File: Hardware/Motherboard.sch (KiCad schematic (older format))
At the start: 19 parts, among them J1 Pin_Header_02x08, J2 Pin_Header_02x08, J3 Pin_Header_02x08, U1 PIC18F26K22-I-SO, U2 FT240XS, U3 TXB0104D, U4 TXB0104D

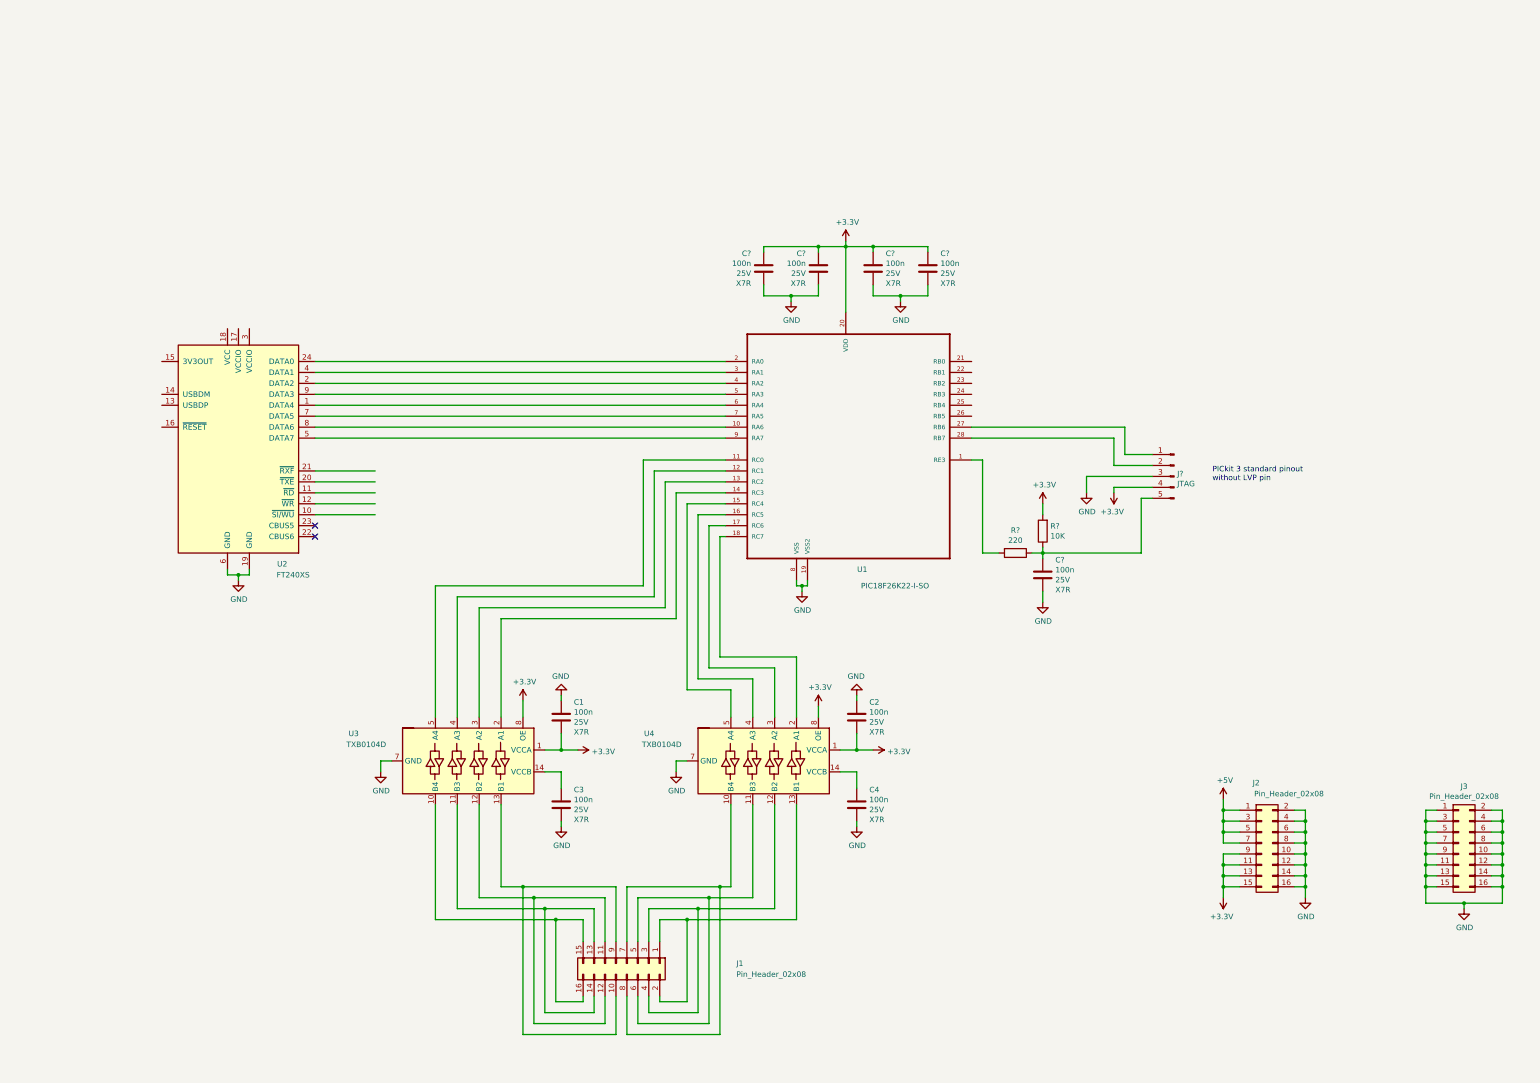
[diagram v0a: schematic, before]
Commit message: [Hardware] Added LDO and led to schematic.
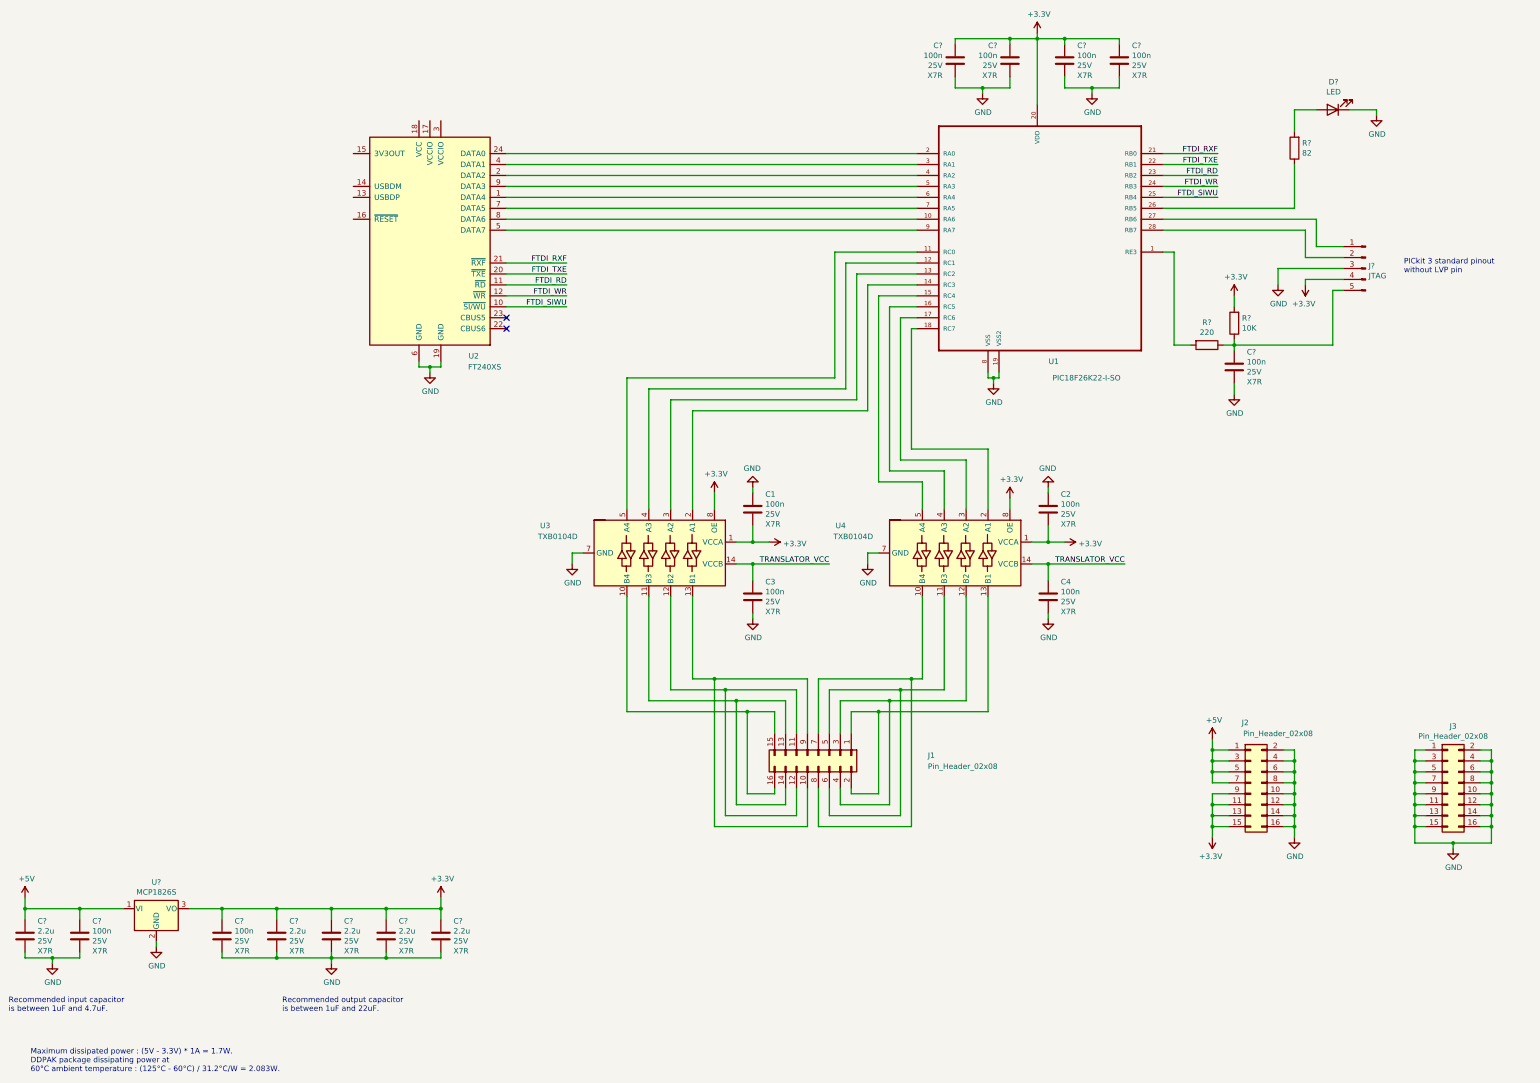
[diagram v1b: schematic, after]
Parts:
- added C? (x2): 100n, Capacitor_SMD:C_1206_3216Metric_Pad1.42x1.75mm_HandSolder, symbol Device:C
- added C? (x5): 2.2u, Capacitor_SMD:C_1206_3216Metric_Pad1.42x1.75mm_HandSolder, symbol Device:C
- added D?: LED, LED_THT:LED_D5.0mm, symbol Device:LED
- added R?: 82, Resistor_SMD:R_1206_3216Metric_Pad1.42x1.75mm_HandSolder, symbol Device:R
- added U?: MCP1826S, Package_TO_SOT_SMD:TO-263-3_TabPin2, symbol Regulator_Linear:MCP1826S
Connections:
- net +3V3: now also C?.1, C?.1, C?.1, C?.1, C?.1, U?.3 (VO)
- net +5V: now also C?.1, C?.1, U?.1 (VI)
- net GND: now also C?.2, C?.2, C?.2, C?.2, C?.2, C?.2, C?.2, D?.1 (K), U?.2 (GND)
- net FTDI_SIWU: now reaches U2.10 (~SI/WU)
- net FTDI_SIWU: now also U1.25 (RB4)
- net FTDI_RD: now reaches U2.11 (~RD)
- net FTDI_RD: now also U1.23 (RB2)
- net FTDI_WR: now reaches U2.12 (~WR)
- net FTDI_WR: now also U1.24 (RB3)
- net FTDI_TXE: now reaches U2.20 (~TXE)
- net FTDI_TXE: now also U1.22 (RB1)
- net FTDI_RXF: now reaches U2.21 (~RXF)
- net FTDI_RXF: now also U1.21 (RB0)
- net at U1.26 (RB5): now also R?.1
- net TRANSLATOR_VCC: now reaches C3.1, U3.14 (VCCB)
- net TRANSLATOR_VCC: now also C4.1, U4.14 (VCCB)
- new net: D?.2 (A), R?.2
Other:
- note added: "Maximum dissipated power : (5V - 3.3V) * 1A = 1.7W.\nDDPAK package dissipating power at\n60°C ambient temperature : (125°C - 60°C) / 31.2°C/W = 2.083W."
- note added: "Recommended input capacitor\nis between 1uF and 4.7uF."
- note added: "Recommended output capacitor\nis between 1uF and 22uF."
- moved on the sheet: C1, C2, C3, C4, C?, J1, J2, J3, J?, R?, U1, U2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

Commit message: [Hardware] Added FTDI FIFO and logic signals output voltage switch to schematic.
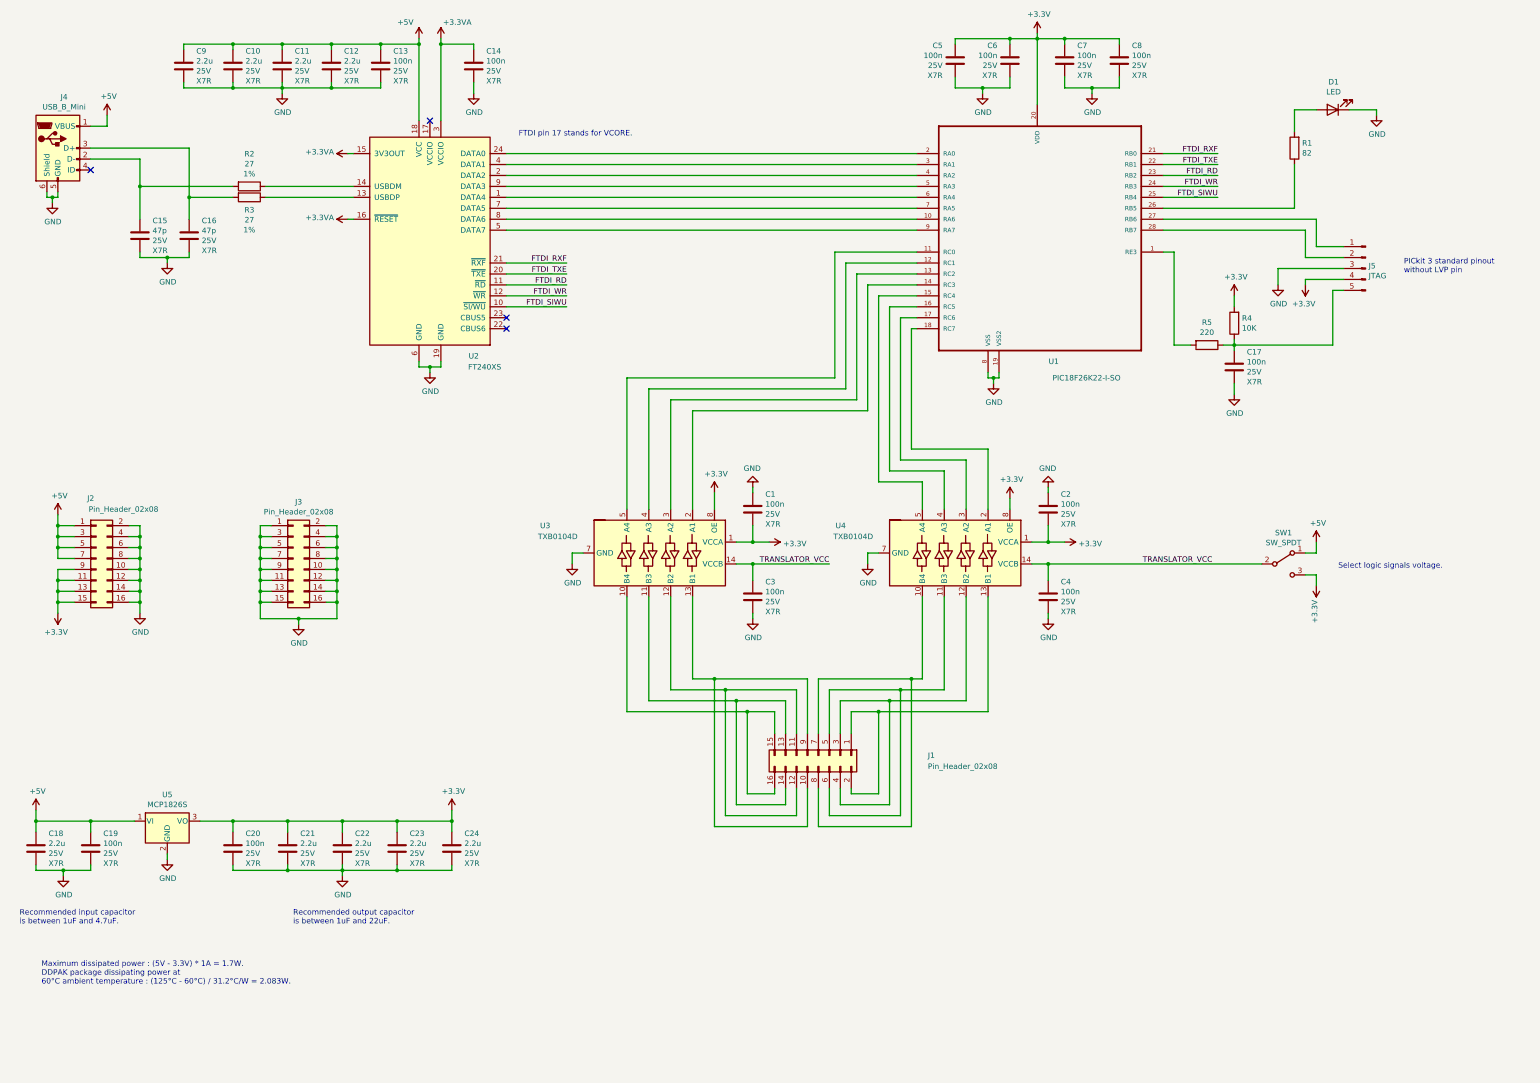
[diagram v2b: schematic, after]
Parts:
- added C10, C11, C12, C9: 2.2u, Capacitor_SMD:C_1206_3216Metric_Pad1.42x1.75mm_HandSolder, symbol Device:C
- added C13, C14: 100n, Capacitor_SMD:C_1206_3216Metric_Pad1.42x1.75mm_HandSolder, symbol Device:C
- added C15, C16: 47p, Capacitor_SMD:C_1206_3216Metric_Pad1.42x1.75mm_HandSolder, symbol Device:C
- added J4: USB_B_Mini, Connector_USB:USB_Mini-B_Lumberg_2486_01_Horizontal, symbol Connector:USB_B_Mini
- added R2, R3: 27, Resistor_SMD:R_1206_3216Metric_Pad1.42x1.75mm_HandSolder, symbol Device:R
- added SW1: SW_SPDT, Button_Switch_THT:SW_CuK_OS102011MA1QN1_SPDT_Angled, symbol Switch:SW_SPDT
- gave numbers to parts that had none: 18
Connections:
- net +3V3: now also SW1.3 (C)
- net +5V: now also U2.18 (VCC), C10.1, C11.1, C12.1, C13.1, C9.1, J4.1 (VBUS), SW1.1 (A)
- net GND: now also C10.2, C11.2, C12.2, C13.2, C14.2, C15.2, C16.2, C9.2, J4.5 (GND), J4.6 (Shield)
- net TRANSLATOR_VCC: now also SW1.2 (B)
- net at U2.13 (USBDP): now also R3.1
- net at U2.14 (USBDM): now also R2.1
- net +3.3VA: now reaches U2.15 (3V3OUT)
- net +3.3VA: now also U2.16 (~RESET), U2.3 (VCCIO), C14.1
- new net: C15.1, J4.2 (D-), R2.2
- new net: C16.1, J4.3 (D+), R3.2
- no-connect marks 2 -> 4
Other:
- note added: "FTDI pin 17 stands for VCORE."
- note added: "Select logic signals voltage."
- moved on the sheet: C18, C19, C20, C21, C22, C23, C24, J2, J3, U5

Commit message: [Hardware] Placed components on PCB.
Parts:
- C1, C10, C11, C12, C13, C14, C15, C16, C17, C18, C19, C2, C20, C21, C22, C23, C24, C3, C4, C5, C6, C7, C8, C9: footprint Capacitor_SMD:C_1206_3216Metric_Pad1.42x1.75mm_HandSolder -> Capacitor_SMD:C_0805_2012Metric_Pad1.15x1.40mm_HandSolder
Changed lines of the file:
@@
 F 0 "C2" H 11265 5887 50  0000 L CNN
 F 1 "100n" H 11265 5796 50  0000 L CNN
-F 2 "Capacitor_SMD:C_1206_3216Metric_Pad1.42x1.75mm_HandSolder" H 11188 5600 50  0001 C CNN
+F 2 "Capacitor_SMD:C_0805_2012Metric_Pad1.15x1.40mm_HandSolder" H 11188 5600 50  0001 C CNN
 F 3 "~" H 11150 5750 50  0001 C CNN
 F 4 "25V" H 11265 5705 50  0000 L CNN "Value2"
@@
 F 0 "C4" H 11265 6687 50  0000 L CNN
 F 1 "100n" H 11265 6596 50  0000 L CNN
-F 2 "Capacitor_SMD:C_1206_3216Metric_Pad1.42x1.75mm_HandSolder" H 11188 6400 50  0001 C CNN
+F 2 "Capacitor_SMD:C_0805_2012Metric_Pad1.15x1.40mm_HandSolder" H 11188 6400 50  0001 C CNN
 F 3 "~" H 11150 6550 50  0001 C CNN
 F 4 "25V" H 11265 6505 50  0000 L CNN "Value2"
@@
 F 0 "C1" H 8565 5887 50  0000 L CNN
 F 1 "100n" H 8565 5796 50  0000 L CNN
-F 2 "Capacitor_SMD:C_1206_3216Metric_Pad1.42x1.75mm_HandSolder" H 8488 5600 50  0001 C CNN
+F 2 "Capacitor_SMD:C_0805_2012Metric_Pad1.15x1.40mm_HandSolder" H 8488 5600 50  0001 C CNN
 F 3 "~" H 8450 5750 50  0001 C CNN
 F 4 "25V" H 8565 5705 50  0000 L CNN "Value2"
@@
 F 0 "C3" H 8565 6687 50  0000 L CNN
 F 1 "100n" H 8565 6596 50  0000 L CNN
-F 2 "Capacitor_SMD:C_1206_3216Metric_Pad1.42x1.75mm_HandSolder" H 8488 6400 50  0001 C CNN
+F 2 "Capacitor_SMD:C_0805_2012Metric_Pad1.15x1.40mm_HandSolder" H 8488 6400 50  0001 C CNN
 F 3 "~" H 8450 6550 50  0001 C CNN
 F 4 "25V" H 8565 6505 50  0000 L CNN "Value2"
@@
 F 0 "C7" H 11415 1787 50  0000 L CNN
 F 1 "100n" H 11415 1696 50  0000 L CNN
-F 2 "Capacitor_SMD:C_1206_3216Metric_Pad1.42x1.75mm_HandSolder" H 11338 1500 50  0001 C CNN
+F 2 "Capacitor_SMD:C_0805_2012Metric_Pad1.15x1.40mm_HandSolder" H 11338 1500 50  0001 C CNN
 F 3 "~" H 11300 1650 50  0001 C CNN
 F 4 "25V" H 11415 1605 50  0000 L CNN "Value2"
@@
 F 0 "C8" H 11915 1787 50  0000 L CNN
 F 1 "100n" H 11915 1696 50  0000 L CNN
-F 2 "Capacitor_SMD:C_1206_3216Metric_Pad1.42x1.75mm_HandSolder" H 11838 1500 50  0001 C CNN
+F 2 "Capacitor_SMD:C_0805_2012Metric_Pad1.15x1.40mm_HandSolder" H 11838 1500 50  0001 C CNN
 F 3 "~" H 11800 1650 50  0001 C CNN
 F 4 "25V" H 11915 1605 50  0000 L CNN "Value2"
@@
 F 0 "C5" H 10185 1787 50  0000 R CNN
 F 1 "100n" H 10185 1696 50  0000 R CNN
-F 2 "Capacitor_SMD:C_1206_3216Metric_Pad1.42x1.75mm_HandSolder" H 10338 1500 50  0001 C CNN
+F 2 "Capacitor_SMD:C_0805_2012Metric_Pad1.15x1.40mm_HandSolder" H 10338 1500 50  0001 C CNN
 F 3 "~" H 10300 1650 50  0001 C CNN
 F 4 "25V" H 10185 1605 50  0000 R CNN "Value2"
@@
 F 0 "C6" H 10685 1787 50  0000 R CNN
 F 1 "100n" H 10685 1696 50  0000 R CNN
-F 2 "Capacitor_SMD:C_1206_3216Metric_Pad1.42x1.75mm_HandSolder" H 10838 1500 50  0001 C CNN
+F 2 "Capacitor_SMD:C_0805_2012Metric_Pad1.15x1.40mm_HandSolder" H 10838 1500 50  0001 C CNN
 F 3 "~" H 10800 1650 50  0001 C CNN
 F 4 "25V" H 10685 1605 50  0000 R CNN "Value2"
@@
 F 0 "C17" H 12965 4587 50  0000 L CNN
 F 1 "100n" H 12965 4496 50  0000 L CNN
-F 2 "Capacitor_SMD:C_1206_3216Metric_Pad1.42x1.75mm_HandSolder" H 12888 4300 50  0001 C CNN
+F 2 "Capacitor_SMD:C_0805_2012Metric_Pad1.15x1.40mm_HandSolder" H 12888 4300 50  0001 C CNN
 F 3 "~" H 12850 4450 50  0001 C CNN
 F 4 "25V" H 12965 4405 50  0000 L CNN "Champ4"
@@
 F 0 "C19" H 2515 8987 50  0000 L CNN
 F 1 "100n" H 2515 8896 50  0000 L CNN
-F 2 "Capacitor_SMD:C_1206_3216Metric_Pad1.42x1.75mm_HandSolder" H 2438 8700 50  0001 C CNN
+F 2 "Capacitor_SMD:C_0805_2012Metric_Pad1.15x1.40mm_HandSolder" H 2438 8700 50  0001 C CNN
 F 3 "~" H 2400 8850 50  0001 C CNN
 F 4 "25V" H 2515 8805 50  0000 L CNN "Value2"
@@
 F 0 "C20" H 3815 8987 50  0000 L CNN
 F 1 "100n" H 3815 8896 50  0000 L CNN
-F 2 "Capacitor_SMD:C_1206_3216Metric_Pad1.42x1.75mm_HandSolder" H 3738 8700 50  0001 C CNN
+F 2 "Capacitor_SMD:C_0805_2012Metric_Pad1.15x1.40mm_HandSolder" H 3738 8700 50  0001 C CNN
 F 3 "~" H 3700 8850 50  0001 C CNN
 F 4 "25V" H 3815 8805 50  0000 L CNN "Value2"
@@
 F 0 "C21" H 4315 8987 50  0000 L CNN
 F 1 "2.2u" H 4315 8896 50  0000 L CNN
-F 2 "Capacitor_SMD:C_1206_3216Metric_Pad1.42x1.75mm_HandSolder" H 4238 8700 50  0001 C CNN
+F 2 "Capacitor_SMD:C_0805_2012Metric_Pad1.15x1.40mm_HandSolder" H 4238 8700 50  0001 C CNN
 F 3 "~" H 4200 8850 50  0001 C CNN
 F 4 "25V" H 4315 8805 50  0000 L CNN "Value2"
@@
 F 0 "C18" H 2015 8987 50  0000 L CNN
 F 1 "2.2u" H 2015 8896 50  0000 L CNN
-F 2 "Capacitor_SMD:C_1206_3216Metric_Pad1.42x1.75mm_HandSolder" H 1938 8700 50  0001 C CNN
+F 2 "Capacitor_SMD:C_0805_2012Metric_Pad1.15x1.40mm_HandSolder" H 1938 8700 50  0001 C CNN
 F 3 "~" H 1900 8850 50  0001 C CNN
 F 4 "25V" H 2015 8805 50  0000 L CNN "Value2"
@@
 F 0 "C22" H 4815 8987 50  0000 L CNN
 F 1 "2.2u" H 4815 8896 50  0000 L CNN
-F 2 "Capacitor_SMD:C_1206_3216Metric_Pad1.42x1.75mm_HandSolder" H 4738 8700 50  0001 C CNN
+F 2 "Capacitor_SMD:C_0805_2012Metric_Pad1.15x1.40mm_HandSolder" H 4738 8700 50  0001 C CNN
 F 3 "~" H 4700 8850 50  0001 C CNN
 F 4 "25V" H 4815 8805 50  0000 L CNN "Value2"
@@
 F 0 "C23" H 5315 8987 50  0000 L CNN
 F 1 "2.2u" H 5315 8896 50  0000 L CNN
-F 2 "Capacitor_SMD:C_1206_3216Metric_Pad1.42x1.75mm_HandSolder" H 5238 8700 50  0001 C CNN
+F 2 "Capacitor_SMD:C_0805_2012Metric_Pad1.15x1.40mm_HandSolder" H 5238 8700 50  0001 C CNN
 F 3 "~" H 5200 8850 50  0001 C CNN
 F 4 "25V" H 5315 8805 50  0000 L CNN "Value2"
@@
 F 0 "C24" H 5815 8987 50  0000 L CNN
 F 1 "2.2u" H 5815 8896 50  0000 L CNN
-F 2 "Capacitor_SMD:C_1206_3216Metric_Pad1.42x1.75mm_HandSolder" H 5738 8700 50  0001 C CNN
+F 2 "Capacitor_SMD:C_0805_2012Metric_Pad1.15x1.40mm_HandSolder" H 5738 8700 50  0001 C CNN
 F 3 "~" H 5700 8850 50  0001 C CNN
 F 4 "25V" H 5815 8805 50  0000 L CNN "Value2"
@@
 F 0 "C14" H 6015 1837 50  0000 L CNN
 F 1 "100n" H 6015 1746 50  0000 L CNN
-F 2 "Capacitor_SMD:C_1206_3216Metric_Pad1.42x1.75mm_HandSolder" H 5938 1550 50  0001 C CNN
+F 2 "Capacitor_SMD:C_0805_2012Metric_Pad1.15x1.40mm_HandSolder" H 5938 1550 50  0001 C CNN
 F 3 "~" H 5900 1700 50  0001 C CNN
 F 4 "25V" H 6015 1655 50  0000 L CNN "Value2"
@@
 F 0 "C13" H 5165 1837 50  0000 L CNN
 F 1 "100n" H 5165 1746 50  0000 L CNN
-F 2 "Capacitor_SMD:C_1206_3216Metric_Pad1.42x1.75mm_HandSolder" H 5088 1550 50  0001 C CNN
+F 2 "Capacitor_SMD:C_0805_2012Metric_Pad1.15x1.40mm_HandSolder" H 5088 1550 50  0001 C CNN
 F 3 "~" H 5050 1700 50  0001 C CNN
 F 4 "25V" H 5165 1655 50  0000 L CNN "Value2"
@@
 F 0 "C12" H 4715 1837 50  0000 L CNN
 F 1 "2.2u" H 4715 1746 50  0000 L CNN
-F 2 "Capacitor_SMD:C_1206_3216Metric_Pad1.42x1.75mm_HandSolder" H 4638 1550 50  0001 C CNN
+F 2 "Capacitor_SMD:C_0805_2012Metric_Pad1.15x1.40mm_HandSolder" H 4638 1550 50  0001 C CNN
 F 3 "~" H 4600 1700 50  0001 C CNN
 F 4 "25V" H 4715 1655 50  0000 L CNN "Value2"
@@
 F 0 "C11" H 4265 1837 50  0000 L CNN
 F 1 "2.2u" H 4265 1746 50  0000 L CNN
-F 2 "Capacitor_SMD:C_1206_3216Metric_Pad1.42x1.75mm_HandSolder" H 4188 1550 50  0001 C CNN
+F 2 "Capacitor_SMD:C_0805_2012Metric_Pad1.15x1.40mm_HandSolder" H 4188 1550 50  0001 C CNN
 F 3 "~" H 4150 1700 50  0001 C CNN
 F 4 "25V" H 4265 1655 50  0000 L CNN "Value2"
@@
 F 0 "C10" H 3815 1837 50  0000 L CNN
 F 1 "2.2u" H 3815 1746 50  0000 L CNN
-F 2 "Capacitor_SMD:C_1206_3216Metric_Pad1.42x1.75mm_HandSolder" H 3738 1550 50  0001 C CNN
+F 2 "Capacitor_SMD:C_0805_2012Metric_Pad1.15x1.40mm_HandSolder" H 3738 1550 50  0001 C CNN
 F 3 "~" H 3700 1700 50  0001 C CNN
 F 4 "25V" H 3815 1655 50  0000 L CNN "Value2"
@@
 F 0 "C9" H 3365 1837 50  0000 L CNN
 F 1 "2.2u" H 3365 1746 50  0000 L CNN
-F 2 "Capacitor_SMD:C_1206_3216Metric_Pad1.42x1.75mm_HandSolder" H 3288 1550 50  0001 C CNN
+F 2 "Capacitor_SMD:C_0805_2012Metric_Pad1.15x1.40mm_HandSolder" H 3288 1550 50  0001 C CNN
 F 3 "~" H 3250 1700 50  0001 C CNN
 F 4 "25V" H 3365 1655 50  0000 L CNN "Value2"
@@
 F 0 "C16" H 3415 3387 50  0000 L CNN
 F 1 "47p" H 3415 3296 50  0000 L CNN
-F 2 "Capacitor_SMD:C_1206_3216Metric_Pad1.42x1.75mm_HandSolder" H 3338 3100 50  0001 C CNN
+F 2 "Capacitor_SMD:C_0805_2012Metric_Pad1.15x1.40mm_HandSolder" H 3338 3100 50  0001 C CNN
 F 3 "~" H 3300 3250 50  0001 C CNN
 F 4 "25V" H 3415 3205 50  0000 L CNN "Value2"
@@
 F 0 "C15" H 2965 3387 50  0000 L CNN
 F 1 "47p" H 2965 3296 50  0000 L CNN
-F 2 "Capacitor_SMD:C_1206_3216Metric_Pad1.42x1.75mm_HandSolder" H 2888 3100 50  0001 C CNN
+F 2 "Capacitor_SMD:C_0805_2012Metric_Pad1.15x1.40mm_HandSolder" H 2888 3100 50  0001 C CNN
 F 3 "~" H 2850 3250 50  0001 C CNN
 F 4 "25V" H 2965 3205 50  0000 L CNN "Value2"
